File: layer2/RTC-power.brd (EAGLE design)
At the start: 17.8 x 49.5 mm, 15 parts, among them U1 DS3234, U2 MCP73831

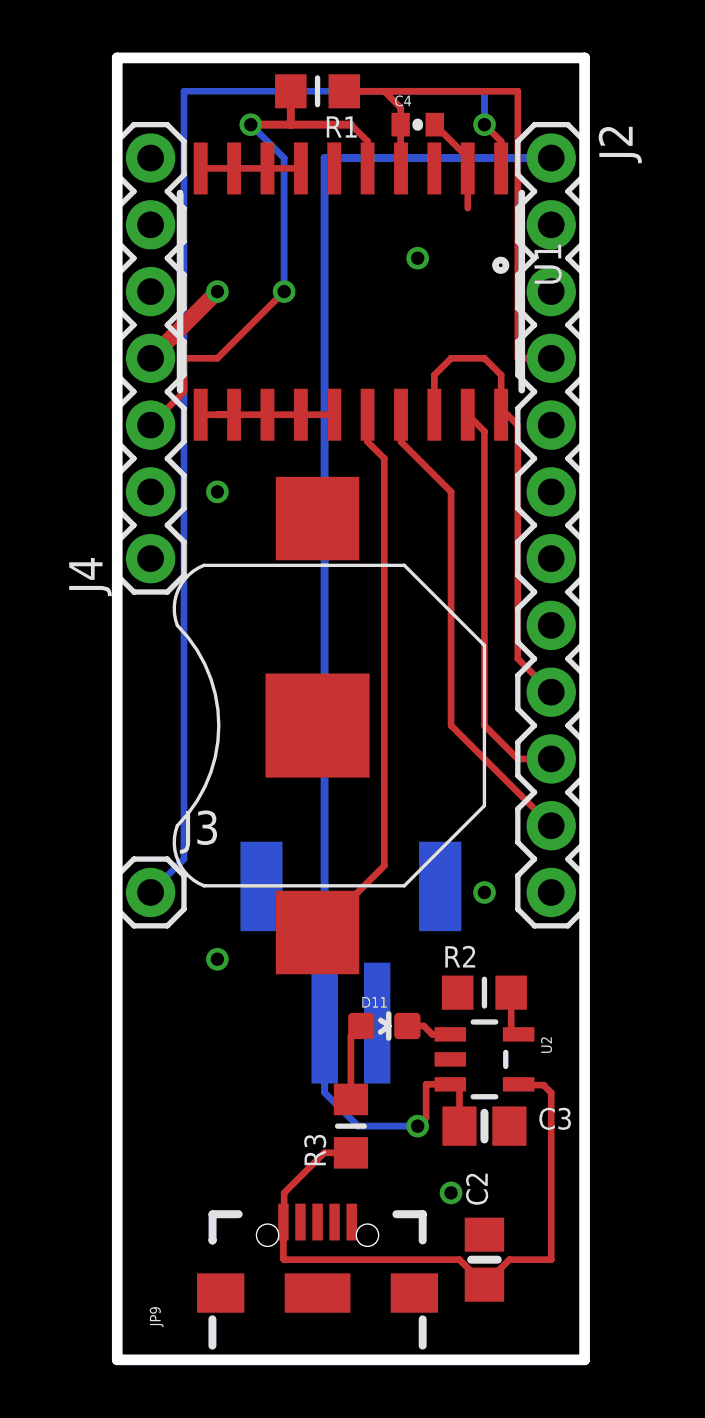
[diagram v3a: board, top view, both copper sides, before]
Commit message: silk screen adjustment
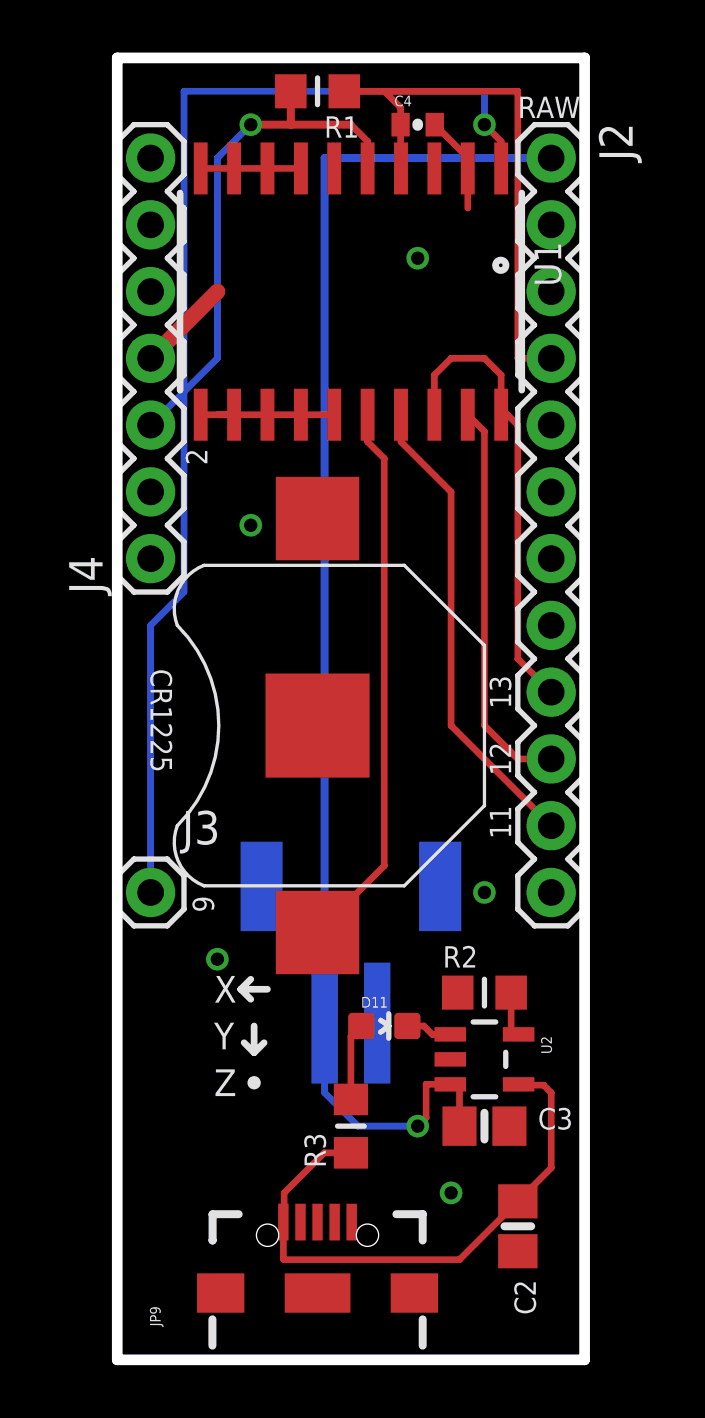
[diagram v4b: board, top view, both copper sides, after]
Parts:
- moved C2 1.80 mm to (15.2, 5.08), turned to 270 degrees
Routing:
- net VIN: track 24.5 -> 21.6 mm
- net INT/SQW: track 21.8 -> 20.0 mm, vias 2 -> 1
- net GND: vias 6 -> 5
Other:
- board text added: "11"
- board text added: "12"
- board text added: "13"
- board text added: "2"
- board text added: "9"
- board text added: "CR1225"
- board text added: "RAW"
- board text added: "X"
- board text added: "Y"
- board text added: "Z"
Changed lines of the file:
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@@
 <wire x1="17.78" y1="49.53" x2="17.78" y2="0" width="0.4064" layer="20"/>
 <wire x1="0" y1="0" x2="17.78" y2="0" width="0.4064" layer="20"/>
+<wire x1="5.207" y1="11.684" x2="5.207" y2="12.7" width="0.254" layer="21"/>
+<wire x1="5.207" y1="11.684" x2="5.588" y2="12.065" width="0.254" layer="21"/>
+<wire x1="5.207" y1="11.684" x2="4.826" y2="12.065" width="0.254" layer="21"/>
+<wire x1="4.699" y1="14.097" x2="5.715" y2="14.097" width="0.254" layer="21"/>
+<wire x1="4.699" y1="14.097" x2="5.08" y2="13.716" width="0.254" layer="21"/>
+<wire x1="4.699" y1="14.097" x2="5.08" y2="14.478" width="0.254" layer="21"/>
+<circle x="5.207" y="10.541" radius="0.127" width="0.254" layer="21"/>
+<text x="3.683" y="13.589" size="1.016" layer="21" font="vector" ratio="15">X</text>
+<text x="3.683" y="11.811" size="1.016" layer="21" font="vector" ratio="15">Y</text>
+<text x="3.683" y="10.033" size="1.016" layer="21" font="vector" ratio="15">Z</text>
+<text x="3.683" y="17.018" size="0.8128" layer="21" font="vector" ratio="15" rot="R90">9</text>
+<text x="14.986" y="19.812" size="0.8128" layer="21" font="vector" ratio="15" rot="R90">11</text>
+<text x="14.986" y="22.225" size="0.8128" layer="21" font="vector" ratio="15" rot="R90">12</text>
+<text x="14.986" y="24.765" size="0.8128" layer="21" font="vector" ratio="15" rot="R90">13</text>
+<text x="15.24" y="47.244" size="0.8128" layer="21" font="vector" ratio="15">RAW</text>
+<text x="1.27" y="26.289" size="0.8128" layer="21" font="vector" ratio="15" rot="SR270">CR1225</text>
+<text x="3.429" y="34.036" size="0.8128" layer="21" font="vector" ratio="15" rot="R90">2</text>
 </plain>
 <attributes>
@@
 <element name="R3" library="microbuilder" package="_0805MP" value="330" x="8.89" y="8.89" rot="R90"/>
 <element name="R2" library="microbuilder" package="_0805MP" value="2.0k" x="13.97" y="13.97"/>
-<element name="C2" library="microbuilder" package="0805-NO" value="4.7uF" x="13.97" y="3.81" rot="R90"/>
+<element name="C2" library="microbuilder" package="0805-NO" value="4.7uF" x="15.24" y="5.08" rot="R270"/>
 <element name="C3" library="microbuilder" package="0805-NO" value="4.7uF" x="13.97" y="8.89"/>
 <element name="C4" library="SparkFun" package="0402-CAP" value="22pF" x="11.43" y="46.99"/>
@@
 <wire x1="13.97" y1="46.99" x2="13.97" y2="48.26" width="0.254" layer="16"/>
 <wire x1="13.97" y1="48.26" x2="2.54" y2="48.26" width="0.254" layer="16"/>
-<wire x1="2.54" y1="48.26" x2="2.54" y2="19.05" width="0.254" layer="16"/>
-<wire x1="2.54" y1="19.05" x2="1.27" y2="17.78" width="0.254" layer="16"/>
 <wire x1="14.605" y1="45.325" x2="14.605" y2="46.355" width="0.254" layer="1"/>
 <wire x1="14.605" y1="46.355" x2="13.97" y2="46.99" width="0.254" layer="1"/>
 <contactref element="J3" pad="1"/>
+<wire x1="1.27" y1="17.78" x2="1.27" y2="27.94" width="0.254" layer="16"/>
+<wire x1="1.27" y1="27.94" x2="2.54" y2="29.21" width="0.254" layer="16"/>
+<wire x1="2.54" y1="29.21" x2="2.54" y2="48.26" width="0.254" layer="16"/>
 </signal>
 <signal name="GND">
@@
 <wire x1="3.81" y1="35.955" x2="4.445" y2="35.955" width="0.254" layer="1"/>
 <wire x1="4.445" y1="35.955" x2="3.175" y2="35.955" width="0.254" layer="1"/>
-<via x="3.81" y="33.02" extent="1-16" drill="0.508"/>
+<via x="5.08" y="31.75" extent="1-16" drill="0.508"/>
 <contactref element="C4" pad="2"/>
 <wire x1="13.335" y1="45.325" x2="13.335" y2="45.735" width="0.254" layer="1"/>
@@
 <via x="3.81" y="15.24" extent="1-16" drill="0.508"/>
 <via x="13.97" y="17.78" extent="1-16" drill="0.508"/>
-<via x="3.81" y="40.64" extent="1-16" drill="0.508"/>
 <wire x1="1.27" y1="38.1" x2="3.81" y2="40.64" width="0.6096" layer="1"/>
 <via x="12.7" y="6.35" extent="1-16" drill="0.508"/>
@@
 <wire x1="9.525" y1="45.325" x2="9.525" y2="46.355" width="0.254" layer="1"/>
 <wire x1="9.525" y1="46.355" x2="8.89" y2="46.99" width="0.254" layer="1"/>
-<wire x1="1.27" y1="35.56" x2="2.54" y2="36.83" width="0.254" layer="1"/>
-<wire x1="2.54" y1="36.83" x2="2.54" y2="38.1" width="0.254" layer="1"/>
-<wire x1="2.54" y1="38.1" x2="3.81" y2="38.1" width="0.254" layer="1"/>
-<wire x1="3.81" y1="38.1" x2="6.35" y2="40.64" width="0.254" layer="1"/>
-<via x="6.35" y="40.64" extent="1-16" drill="0.508"/>
-<wire x1="6.35" y1="40.64" x2="6.35" y2="45.72" width="0.254" layer="16"/>
-<wire x1="6.35" y1="45.72" x2="5.08" y2="46.99" width="0.254" layer="16"/>
 <via x="5.08" y="46.99" extent="1-16" drill="0.508"/>
 <wire x1="8.89" y1="46.99" x2="6.604" y2="46.99" width="0.3048" layer="1"/>
@@
 <wire x1="6.604" y1="46.99" x2="5.08" y2="46.99" width="0.3048" layer="1"/>
 <contactref element="J4" pad="3"/>
+<wire x1="1.27" y1="35.56" x2="3.81" y2="38.1" width="0.254" layer="16"/>
+<wire x1="3.81" y1="38.1" x2="3.81" y2="45.72" width="0.254" layer="16"/>
+<wire x1="3.81" y1="45.72" x2="5.08" y2="46.99" width="0.254" layer="16"/>
 </signal>
 <signal name="RTCBATT">
@@
 <wire x1="6.32" y1="5.24" x2="6.32" y2="3.84" width="0.254" layer="1"/>
 <wire x1="6.32" y1="3.84" x2="6.35" y2="3.81" width="0.254" layer="1"/>
-<wire x1="6.35" y1="3.81" x2="13.02" y2="3.81" width="0.254" layer="1"/>
-<wire x1="13.02" y1="3.81" x2="13.97" y2="2.86" width="0.254" layer="1"/>
 <wire x1="8.89" y1="7.874" x2="7.874" y2="7.874" width="0.254" layer="1"/>
 <wire x1="7.874" y1="7.874" x2="6.35" y2="6.35" width="0.254" layer="1"/>
@@
 <wire x1="15.24" y1="10.4499" x2="16.2201" y2="10.4499" width="0.254" layer="1"/>
 <wire x1="16.2201" y1="10.4499" x2="16.51" y2="10.16" width="0.254" layer="1"/>
-<wire x1="16.51" y1="10.16" x2="16.51" y2="3.81" width="0.254" layer="1"/>
-<wire x1="16.51" y1="3.81" x2="14.92" y2="3.81" width="0.254" layer="1"/>
-<wire x1="14.92" y1="3.81" x2="13.97" y2="2.86" width="0.254" layer="1"/>
+<wire x1="6.35" y1="3.81" x2="13.02" y2="3.81" width="0.254" layer="1"/>
+<wire x1="13.02" y1="3.81" x2="15.24" y2="6.03" width="0.254" layer="1"/>
+<wire x1="16.51" y1="10.16" x2="16.51" y2="7.3" width="0.254" layer="1"/>
+<wire x1="16.51" y1="7.3" x2="15.24" y2="6.03" width="0.254" layer="1"/>
 </signal>
 <signal name="SD_CS">

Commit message: silk screen
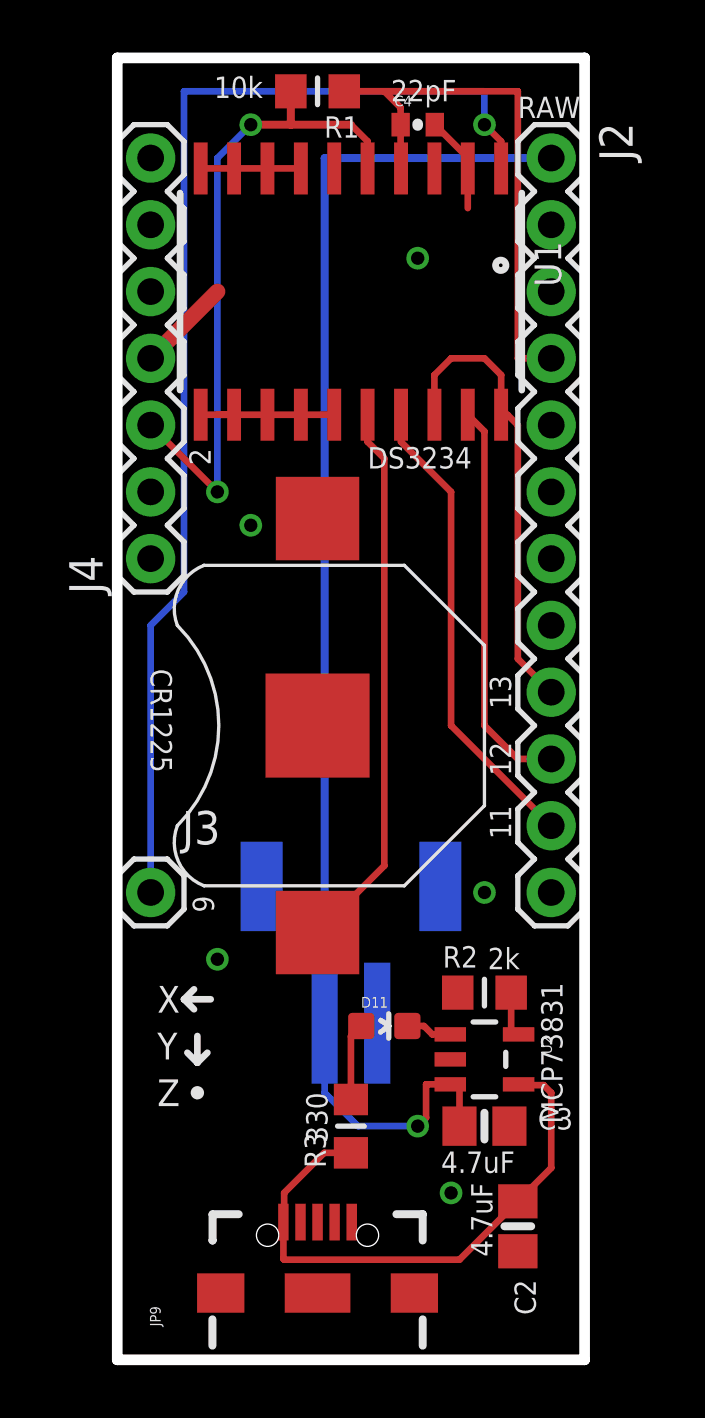
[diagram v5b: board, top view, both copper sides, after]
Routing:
- net INT/SQW: track 20.0 -> 25.2 mm, vias 1 -> 2
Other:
- board text added: "10k"
- board text added: "22pF"
- board text added: "2k"
- board text added: "330"
- board text added: "4.7uF"
- board text added: "DS3234"
- board text added: "MCP73831"
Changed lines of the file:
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@@
 <wire x1="17.78" y1="49.53" x2="17.78" y2="0" width="0.4064" layer="20"/>
 <wire x1="0" y1="0" x2="17.78" y2="0" width="0.4064" layer="20"/>
-<wire x1="5.207" y1="11.684" x2="5.207" y2="12.7" width="0.254" layer="21"/>
-<wire x1="5.207" y1="11.684" x2="5.588" y2="12.065" width="0.254" layer="21"/>
-<wire x1="5.207" y1="11.684" x2="4.826" y2="12.065" width="0.254" layer="21"/>
-<wire x1="4.699" y1="14.097" x2="5.715" y2="14.097" width="0.254" layer="21"/>
-<wire x1="4.699" y1="14.097" x2="5.08" y2="13.716" width="0.254" layer="21"/>
-<wire x1="4.699" y1="14.097" x2="5.08" y2="14.478" width="0.254" layer="21"/>
-<circle x="5.207" y="10.541" radius="0.127" width="0.254" layer="21"/>
-<text x="3.683" y="13.589" size="1.016" layer="21" font="vector" ratio="15">X</text>
-<text x="3.683" y="11.811" size="1.016" layer="21" font="vector" ratio="15">Y</text>
-<text x="3.683" y="10.033" size="1.016" layer="21" font="vector" ratio="15">Z</text>
+<wire x1="3.048" y1="11.303" x2="3.048" y2="12.319" width="0.254" layer="21"/>
+<wire x1="3.048" y1="11.303" x2="3.429" y2="11.684" width="0.254" layer="21"/>
+<wire x1="3.048" y1="11.303" x2="2.667" y2="11.684" width="0.254" layer="21"/>
+<wire x1="2.54" y1="13.716" x2="3.556" y2="13.716" width="0.254" layer="21"/>
+<wire x1="2.54" y1="13.716" x2="2.921" y2="13.335" width="0.254" layer="21"/>
+<wire x1="2.54" y1="13.716" x2="2.921" y2="14.097" width="0.254" layer="21"/>
+<circle x="3.048" y="10.16" radius="0.127" width="0.254" layer="21"/>
+<text x="1.524" y="13.208" size="1.016" layer="21" font="vector" ratio="15">X</text>
+<text x="1.524" y="11.43" size="1.016" layer="21" font="vector" ratio="15">Y</text>
+<text x="1.524" y="9.652" size="1.016" layer="21" font="vector" ratio="15">Z</text>
 <text x="3.683" y="17.018" size="0.8128" layer="21" font="vector" ratio="15" rot="R90">9</text>
 <text x="14.986" y="19.812" size="0.8128" layer="21" font="vector" ratio="15" rot="R90">11</text>
@@
 <text x="15.24" y="47.244" size="0.8128" layer="21" font="vector" ratio="15">RAW</text>
 <text x="1.27" y="26.289" size="0.8128" layer="21" font="vector" ratio="15" rot="SR270">CR1225</text>
-<text x="3.429" y="34.036" size="0.8128" layer="21" font="vector" ratio="15" rot="R90">2</text>
+<text x="3.556" y="34.036" size="0.8128" layer="21" font="vector" ratio="15" rot="R90">2</text>
+<text x="13.462" y="6.731" size="0.8128" layer="21" font="vector" ratio="15" rot="R270">4.7uF</text>
+<text x="12.319" y="7.112" size="0.8128" layer="21" font="vector" ratio="15">4.7uF</text>
+<text x="8.001" y="8.255" size="0.8128" layer="21" font="vector" ratio="15" rot="R90">330</text>
+<text x="14.097" y="14.859" size="0.8128" layer="21" font="vector" ratio="15">2k</text>
+<text x="3.683" y="48.006" size="0.8128" layer="21" font="vector" ratio="15">10k</text>
+<text x="10.414" y="47.879" size="0.8128" layer="21" font="vector" ratio="15">22pF</text>
+<text x="9.525" y="33.909" size="0.8128" layer="21" font="vector" ratio="15">DS3234</text>
+<text x="16.129" y="14.351" size="0.8128" layer="21" font="vector" ratio="15" rot="R270">MCP73831</text>
 </plain>
 <attributes>
@@
 <wire x1="6.604" y1="46.99" x2="5.08" y2="46.99" width="0.3048" layer="1"/>
 <contactref element="J4" pad="3"/>
-<wire x1="1.27" y1="35.56" x2="3.81" y2="38.1" width="0.254" layer="16"/>
-<wire x1="3.81" y1="38.1" x2="3.81" y2="45.72" width="0.254" layer="16"/>
 <wire x1="3.81" y1="45.72" x2="5.08" y2="46.99" width="0.254" layer="16"/>
+<wire x1="1.27" y1="35.56" x2="1.397" y2="35.56" width="0.254" layer="1"/>
+<wire x1="1.397" y1="35.56" x2="1.397" y2="35.433" width="0.254" layer="1"/>
+<wire x1="1.397" y1="35.433" x2="3.81" y2="33.02" width="0.254" layer="1"/>
+<via x="3.81" y="33.02" extent="1-16" drill="0.508"/>
+<wire x1="3.81" y1="33.02" x2="3.81" y2="45.72" width="0.254" layer="16"/>
 </signal>
 <signal name="RTCBATT">

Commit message: increased charging wire width
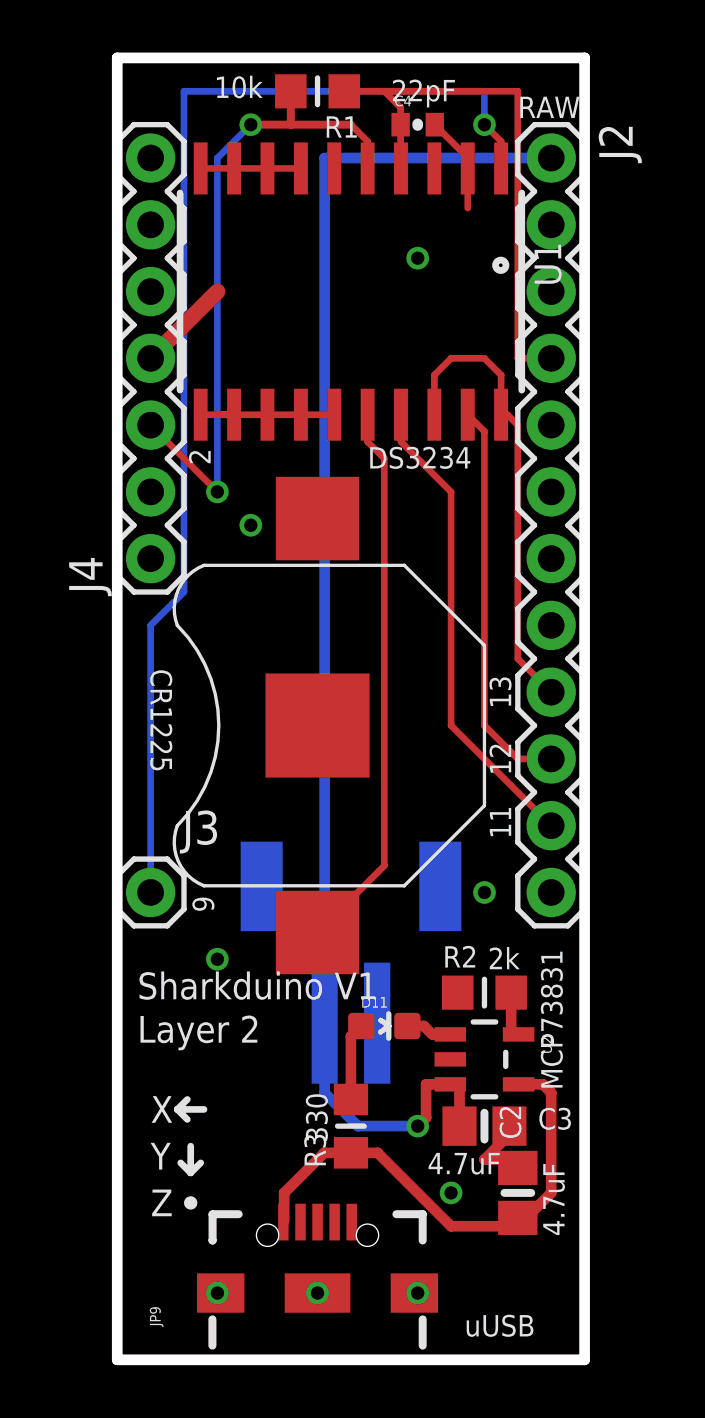
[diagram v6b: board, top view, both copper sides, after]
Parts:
- moved C2 1.27 mm to (15.2, 6.35), turned to 90 degrees
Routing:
- net GND: track 16.8 -> 19.9 mm, vias 5 -> 8
- net VIN: track 21.6 -> 18.8 mm
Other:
- board text added: "Layer 2"
- board text added: "Sharkduino V1"
- board text added: "uUSB"
